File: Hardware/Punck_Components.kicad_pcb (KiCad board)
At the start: 4 copper layers, 91.2 x 99.8 mm, 116 parts, among them J1 Conn_01x12_Female, J2 Conn_01x12_Female, J3 Conn_01x12_Female, J4 Conn_01x12_Female, J5 Debug_Header, J6 SWD_Header, J7 Eurorack_10_pin_power, Q1 MMBT3904, Q2 MMBT3904, Q3 MMBT3904, Q4 MMBT3904, Q5 MMBT3904, Q6 MMBT3904, Q7 MMBT3904, U1 TL074, U2 STM32H743ZITx, U3 W25Q128JVS, U4 PCM5100APW, U5 W25Q128JVS, U6 TPS561201, U7 LD1117-3.3-4Tab, Y1 8MHz 20pF

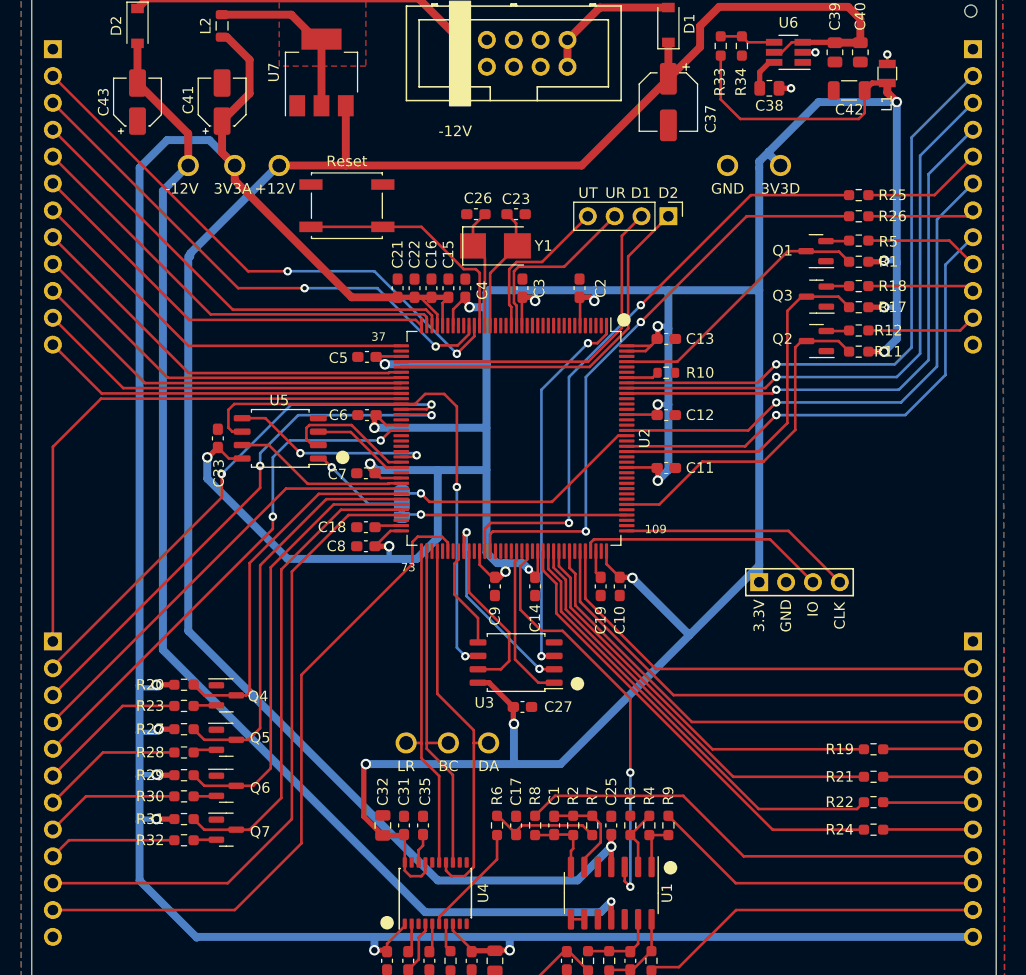
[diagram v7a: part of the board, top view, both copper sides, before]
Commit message: Updated PCBs to match changes in panel; ground returns improved
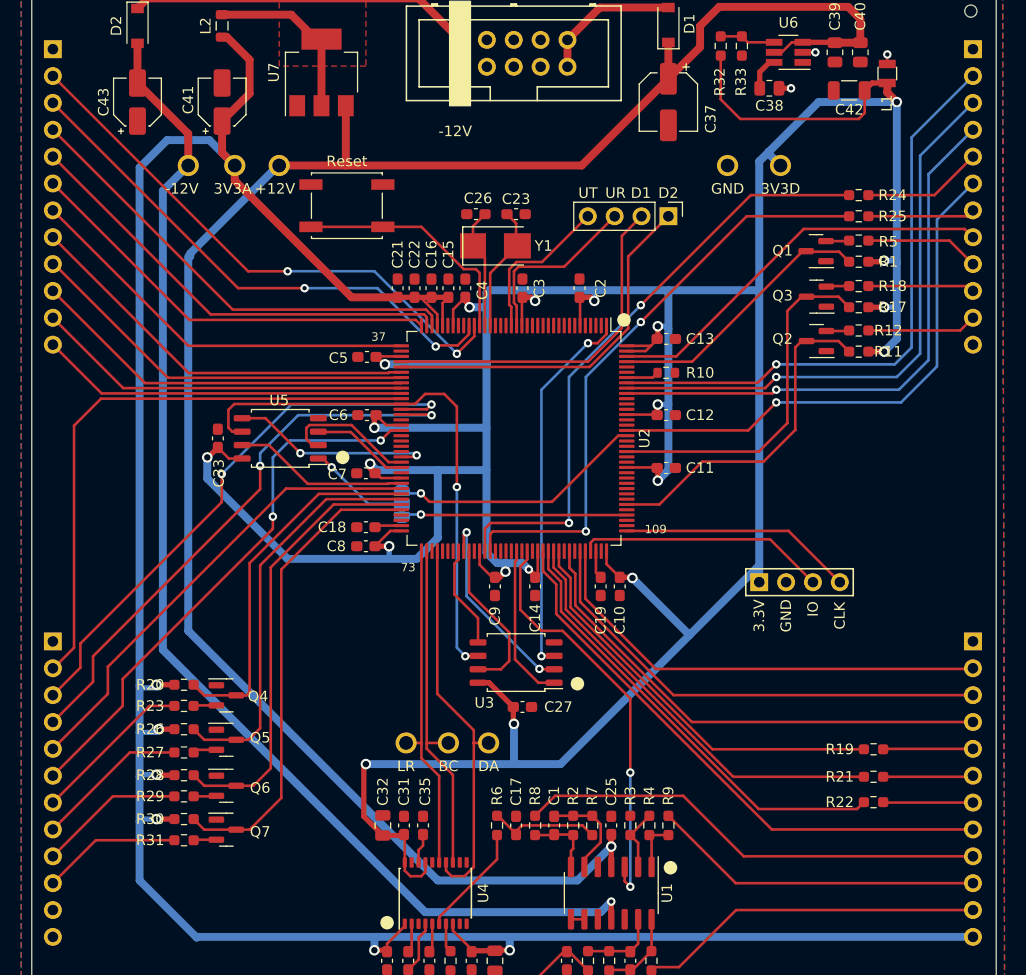
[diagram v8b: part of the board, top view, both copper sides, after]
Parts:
- removed the R24 at (149.6, 129.8)
- renumbered R25 to R24, R26 to R25, R27 to R26, R28 to R27, R29 to R28, R30 to R29, R31 to R30, R32 to R31, R33 to R32, R34 to R33
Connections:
- net /CH_LED renamed /HH_LED
- net /CH_LED_OUT renamed /HH_LED_OUT
- J2 pad 1: /HIHAT_VOL_POT -> GND
- J2 pad 10: /MIDI_LEARN -> /SAMPLER_B_IN
- J2 pad 11: /SEQ_SELECT -> unconnected-(J2-Pad11)
- J2 pad 2: /SAMPLER_A_VOL_POT -> /HIHAT_VOL_POT
- J2 pad 3: /SAMPLER_B_VOL_POT -> /SAMPLER_A_VOL_POT
- J2 pad 4: /CH_BTN -> /SAMPLER_B_VOL_POT
- J2 pad 5: /TEMPO_POT -> /HH_BTN
- J2 pad 6: /CH_IN -> /TEMPO_POT
- J2 pad 7: /OH_IN -> /CH_IN
- J2 pad 8: /SAMPLER_A_IN -> /OH_IN
- J2 pad 9: /SAMPLER_B_IN -> /SAMPLER_A_IN
- J3 pad 8: /OH_BTN -> /MIDI_LEARN
- J4 pad 8: /OH_LED -> /SEQ_SELECT
- U2 pad 125: /OH_BTN -> unconnected-(U2-Pad125)
- U2 pad 142: unconnected-(U2-Pad142) -> /MIDI_LEARN
- U2 pad 64: /CH_BTN -> /HH_BTN
- U2 pad 69: /MIDI_LEARN -> unconnected-(U2-Pad69)
- U2 pad 78: /SEQ_SELECT -> unconnected-(U2-Pad78)
- U2 pad 96: /OH_LED_OUT -> /SEQ_SELECT
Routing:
- net /OH_BTN: track 47.0 -> 0.00 mm, vias 1 -> 0
- net /HH_BTN: track 0.00 -> 44.6 mm
- net /OH_LED_OUT: track 44.0 -> 0.00 mm
- net /CH_BTN: track 42.1 -> 0.00 mm
- net /MIDI_LEARN: track 61.1 -> 38.1 mm
- net /SEQ_SELECT: track 63.6 -> 54.3 mm
- net /OH_LED: track 8.50 -> 0.00 mm
- net /HIHAT_VOL_POT: track 53.2 -> 55.8 mm
- net /TEMPO_POT: track 49.4 -> 51.9 mm
- net /SAMPLER_B_VOL_POT: track 51.6 -> 54.1 mm
- net /SAMPLER_A_VOL_POT: track 50.6 -> 53.1 mm
- net /SAMPLER_B_IN: track 12.1 -> 13.2 mm
- net /OH_IN: track 13.5 -> 14.5 mm
- net /SAMPLER_A_IN: track 12.8 -> 13.8 mm
- net /CH_IN: track 14.2 -> 15.3 mm
